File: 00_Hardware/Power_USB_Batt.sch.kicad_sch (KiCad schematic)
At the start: 38 parts, among them IC1 MAX17048G+T10, J2 USB_C_Receptacle_USB2.0_16P, J4 Header_01x02_2.0mm JST PH, U1 TPS2116DRLR, U2 MIC5219-3.3YM5, U3 USBLC6-2SC6, U4 MCP73831-2-OT

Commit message: Antenna output changed to fully isolate path
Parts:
- removed H1: MountingHole_Pad_M3, MountingHole:MountingHole_3.2mm_M3_DIN965_Pad_TopBottom, symbol IBA_mechanical_parts:MountingHole_Pad_M3
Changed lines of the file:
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@@
 	)
 	(junction
-		(at 208.28 148.59)
-		(diameter 0)
-		(color 0 0 0 0)
-	)
-	(junction
 		(at 80.01 104.14)
 		(diameter 0)
@@
 	(wire
 		(pts
-			(xy 190.5 148.59) (xy 208.28 148.59)
-		)
-		(stroke
-			(width 0)
-			(type default)
-		)
-	)
-	(wire
-		(pts
 			(xy 83.82 104.14) (xy 88.9 104.14)
 		)
@@
 					(unit 1)
 				)
-			)
-		)
-	)
-	(symbol
-		(lib_id "IBA_mechanical_parts:MountingHole_Pad_M3")
-		(at 187.96 148.59 90)
-		(unit 1)
-		(exclude_from_sim no)
-		(in_bom no)
-		(on_board yes)
-		(dnp no)
-		(property "Reference" "H1"
-			(at 181.61 148.59 90)
-			(effects
-				(font
-					(size 1.27 1.27)
-				)
-			)
-		)
-		(property "Value" "MountingHole_Pad_M3"
-			(at 183.515 148.59 0)
-			(effects
-				(font
-					(size 1.27 1.27)
-				)
-				(hide yes)
-			)
-		)
-		(property "Footprint" "MountingHole:MountingHole_3.2mm_M3_DIN965_Pad_TopBottom"
-			(at 179.07 148.59 0)
-			(effects
-				(font
-					(size 1.27 1.27)
-				)
-				(hide yes)
-			)
-		)
-		(property "Datasheet" "~"
-			(at 187.96 148.59 0)
-			(effects
-				(font
-					(size 1.27 1.27)
-				)
-				(hide yes)
-			)
-		)
-		(property "Description" "Mounting Hole with connection, Pad M3"
-			(at 187.96 148.59 0)
-			(effects
-				(font
-					(size 1.27 1.27)
-				)
-				(hide yes)
-			)
-		)
-		(property "MANUFACTURER" ""
-			(at 187.96 148.59 0)
-			(effects
-				(font
-					(size 1.27 1.27)
-				)
-				(hide yes)
-			)
-		)
-		(property "PARTREV" ""
-			(at 187.96 148.59 0)
-			(effects
-				(font
-					(size 1.27 1.27)
-				)
-				(hide yes)
-			)
-		)
-		(property "STANDARD" ""
-			(at 187.96 148.59 0)
-			(effects
-				(font
-					(size 1.27 1.27)
-				)
-				(hide yes)
-			)
-		)
-		(pin "1"
-		)
-		(instances
-			(project ""
-				(path "/179424ee-5b20-4f30-b424-5750e26f83a1/4927cd72-e16a-43de-8cdd-cc75baf4e465"
-					(reference "H1")
-					(unit 1)
-				)

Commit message: updated from generated script
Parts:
- C1, C2: LCSC (none) -> C19702
- IC1: Manufacturer_Name Analog Devices -> (none); Manufacturer_Part_Number MAX17048G+T10 -> (none)
- J2: Mfr1 (none) -> GCT
- R1, R2: value 100K -> 100k
- R10, R9: value 1K5_0805 -> 1.5k
- R11: value 1K_0805 -> 1k
- R12: value 10K0_0603 -> 10k
- R19, R21: value 27 -> 27R
- R3, R4: value 5K1_0805 -> 5.1k
- R5: value 10K -> 10k
- U4: Mfr1 Micochip -> Microchip

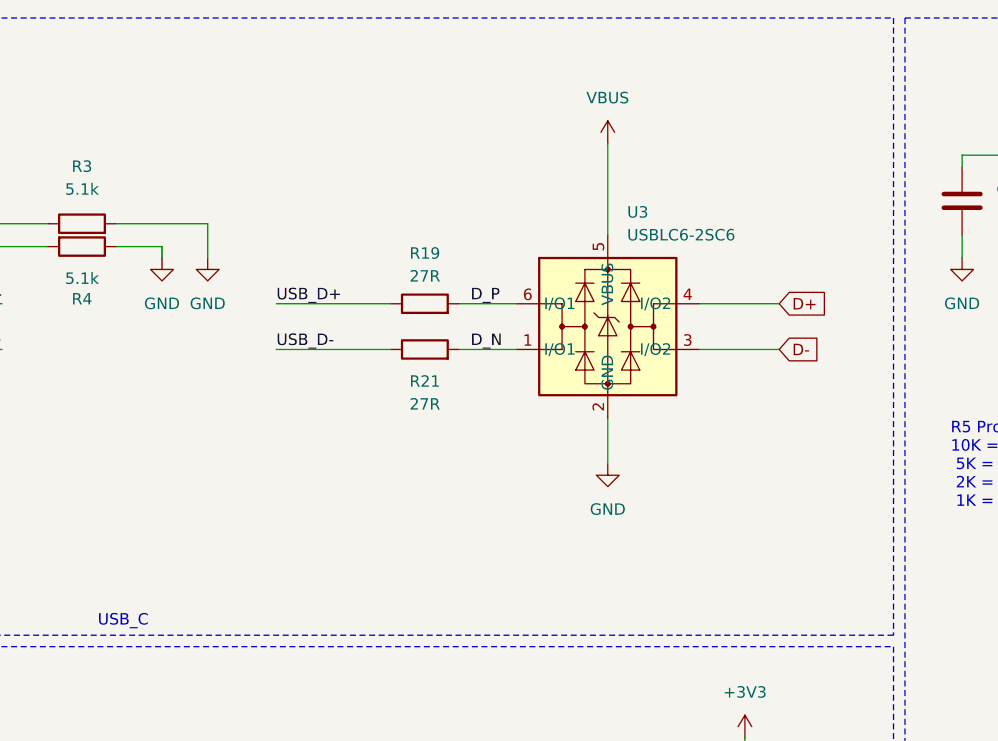
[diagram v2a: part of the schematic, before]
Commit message: Added V1.0 assembly and testing notes, removed traces from ESD to move it V1.1
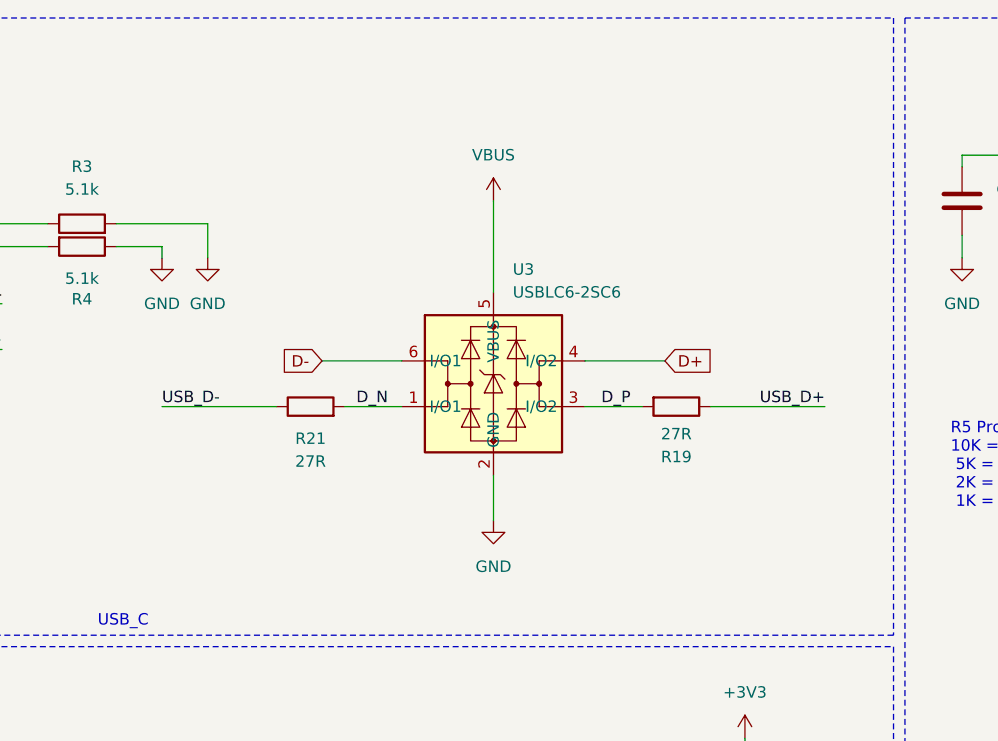
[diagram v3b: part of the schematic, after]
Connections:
- net D-: now also U3.6 (I/O1); no longer U3.3 (I/O2)
- net D_P: now also U3.3 (I/O2); no longer U3.6 (I/O1)
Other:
- moved on the sheet: R19, R21, U3
